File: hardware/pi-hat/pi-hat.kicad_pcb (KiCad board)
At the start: 2 copper layers, 65 x 56 mm, 83 parts, among them J1 PWR IN, J10 6-8, J11 PWM0, J12 PWM1, J13 KLPX-0848A-2-B, J14 KLPX-0848A-2-R, J2 A-F, J3 40HAT, J4 G-M, J5 N-Q, J6 PANEL_PWR, J7 PANEL_CTL, J8 2-5, J9 WP, Q1 DMG2305UX, Q2 DMMT5401, Q3 DMN6075S, Q4 NTR4171P, U1 CAT24C32, U10 L78L33_SOT89, U11 L78L33_SOT89, U12 PCM5122PW, U2 CM1293A, U3 CM1293A, U4 CM1293A, U5 CM1293A, U6 CM1293A, U7 CM1293A, U8 MCP23S17_SO, U9 MCP23S17_SO

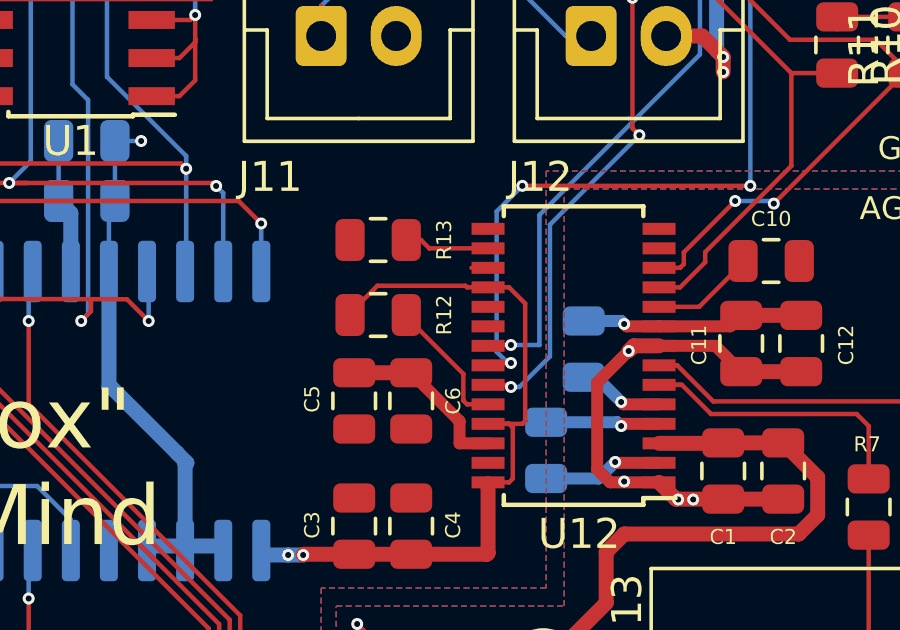
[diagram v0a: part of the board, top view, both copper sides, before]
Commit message: add jumper to optionally bridge pcm_clk and sclk as per datasheet
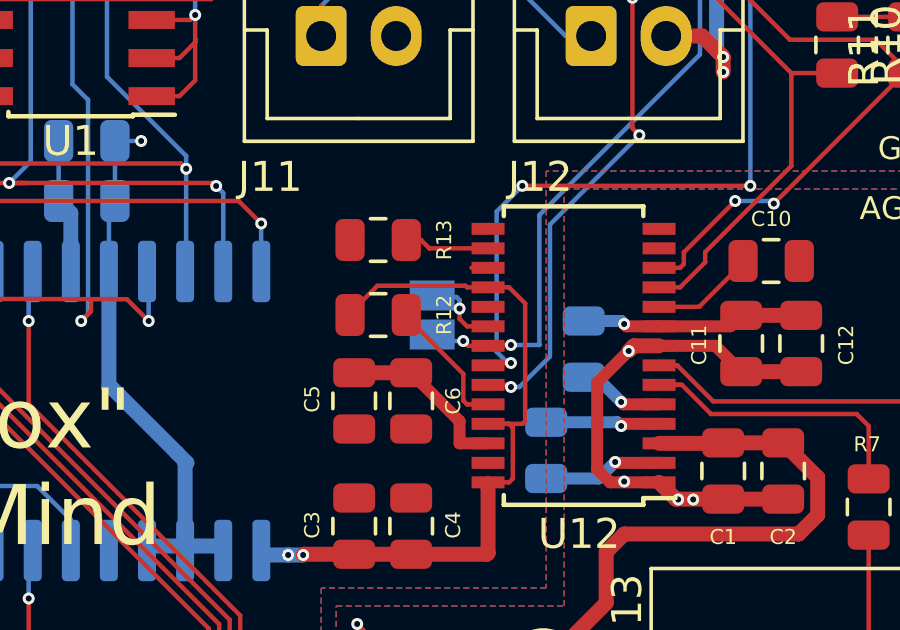
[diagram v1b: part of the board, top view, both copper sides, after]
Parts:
- added JP2: Jumper_NO_Small, Jumper:SolderJumper-2_P1.3mm_Open_Pad1.0x1.5mm, B.Cu at (125.7, 79.8)
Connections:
- U12 pad 20: (no net) -> /DAC_SYSCLK
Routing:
- net /DAC_SYSCLK: track 0.00 -> 2.66 mm, vias 0 -> 1
- net /PCM_CLK: track 58.2 -> 60.2 mm, vias 2 -> 3
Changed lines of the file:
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@@
     (thickness 1.6)
     (drawings 59)
-    (tracks 1117)
+    (tracks 1130)
     (zones 0)
-    (modules 83)
-    (nets 94)
+    (modules 84)
+    (nets 95)
   )
   (page A4)
@@
     (34 B.Paste user hide)
     (35 F.Paste user)
-    (36 B.SilkS user hide)
-    (37 F.SilkS user hide)
+    (36 B.SilkS user)
+    (37 F.SilkS user)
     (38 B.Mask user hide)
     (39 F.Mask user hide)
@@
   )
   (setup
-    (last_trace_width 0.5)
+    (last_trace_width 0.15)
     (user_trace_width 0.15)
     (user_trace_width 0.2)
@@
   (net 92 "Net-(D1-Pad2)")
   (net 93 "Net-(D1-Pad1)")
+  (net 94 /DAC_SYSCLK)
   (net_class Default "This is the default net class."
     (clearance 0.2)
@@
     (add_net /C_IN)
     (add_net /D)
+    (add_net /DAC_SYSCLK)
     (add_net /D_IN)
     (add_net /E)
@@
     (add_net "Net-(D1-Pad1)")
     (add_net "Net-(D1-Pad2)")
+    (add_net "Net-(J1-Pad2)")
+    (add_net "Net-(J1-Pad4)")
+    (add_net "Net-(J3-Pad1)")
+    (add_net "Net-(J3-Pad10)")
+    (add_net "Net-(J3-Pad11)")
+    (add_net "Net-(J3-Pad13)")
+    (add_net "Net-(J3-Pad15)")
+    (add_net "Net-(J3-Pad16)")
+    (add_net "Net-(J3-Pad26)")
+    (add_net "Net-(J3-Pad29)")
+    (add_net "Net-(J3-Pad31)")
+    (add_net "Net-(J3-Pad36)")
+    (add_net "Net-(J3-Pad37)")
+    (add_net "Net-(J3-Pad38)")
+    (add_net "Net-(J3-Pad7)")
+    (add_net "Net-(J3-Pad8)")
+    (add_net "Net-(J6-Pad3)")
+    (add_net "Net-(J7-Pad2)")
     (add_net "Net-(Q1-Pad1)")
     (add_net "Net-(Q2-Pad1)")
     (add_net "Net-(Q3-Pad1)")
     (add_net "Net-(Q4-Pad1)")
+    (add_net "Net-(U12-Pad13)")
+    (add_net "Net-(U12-Pad14)")
+    (add_net "Net-(U12-Pad15)")
+    (add_net "Net-(U12-Pad19)")
+    (add_net "Net-(U8-Pad18)")
+    (add_net "Net-(U8-Pad19)")
+    (add_net "Net-(U9-Pad19)")
+    (add_net "Net-(U9-Pad23)")
+    (add_net "Net-(U9-Pad24)")
+    (add_net "Net-(U9-Pad25)")
+    (add_net "Net-(U9-Pad26)")
+    (add_net "Net-(U9-Pad27)")
+  )
+  (module Jumper:SolderJumper-2_P1.3mm_Open_Pad1.0x1.5mm (layer B.Cu)
+    (at 125.7 79.8 270)
+    (descr "SMD Solder Jumper, 1x1.5mm Pads, 0.3mm gap, open")
+    (tags "solder jumper open")
+    (attr virtual)
+    (fp_text reference JP2 (at 0 1.5 90) (layer B.SilkS)
+      (effects (font (size 0.5 0.5) (thickness 0.125)) (justify mirror))
+    )
+    (fp_text value Jumper_NO_Small (at 0 -1.9 90) (layer B.Fab)
+      (effects (font (size 1 1) (thickness 0.15)) (justify mirror))
+    )
+    (fp_line (start 1.65 -1.25) (end -1.65 -1.25) (layer B.CrtYd) (width 0.05))
+    (fp_line (start 1.65 -1.25) (end 1.65 1.25) (layer B.CrtYd) (width 0.05))
+    (fp_line (start -1.65 1.25) (end -1.65 -1.25) (layer B.CrtYd) (width 0.05))
+    (fp_line (start -1.65 1.25) (end 1.65 1.25) (layer B.CrtYd) (width 0.05))
+    (fp_line (start -1.4 1) (end 1.4 1) (layer B.SilkS) (width 0.12))
+    (fp_line (start 1.4 1) (end 1.4 -1) (layer B.SilkS) (width 0.12))
+    (fp_line (start 1.4 -1) (end -1.4 -1) (layer B.SilkS) (width 0.12))
+    (fp_line (start -1.4 -1) (end -1.4 1) (layer B.SilkS) (width 0.12))
+    (pad 1 smd rect (at -0.65 0 270) (size 1 1.5) (layers B.Cu B.Mask)
+      (net 94 /DAC_SYSCLK))
+    (pad 2 smd rect (at 0.65 0 270) (size 1 1.5) (layers B.Cu B.Mask)
+      (net 75 /PCM_CLK))
   )
   (module TestPoint:TestPoint_Pad_D2.0mm (layer F.Cu)
@@
     (pad 21 smd rect (at 2.85 0.325 180) (size 1.1 0.4) (layers F.Cu F.Paste F.Mask)
       (net 75 /PCM_CLK))
-    (pad 20 smd rect (at 2.85 0.975 180) (size 1.1 0.4) (layers F.Cu F.Paste F.Mask))
+    (pad 20 smd rect (at 2.85 0.975 180) (size 1.1 0.4) (layers F.Cu F.Paste F.Mask)
+      (net 94 /DAC_SYSCLK))
     (pad 19 smd rect (at 2.85 1.625 180) (size 1.1 0.4) (layers F.Cu F.Paste F.Mask))
     (pad 18 smd rect (at 2.85 2.275 180) (size 1.1 0.4) (layers F.Cu F.Paste F.Mask)
@@
   (via (at 84.3 108.6) (size 0.4) (drill 0.2) (layers F.Cu B.Cu) (net 1))
   (via (at 84.8 108.6) (size 0.4) (drill 0.2) (layers F.Cu B.Cu) (net 1))
-  (via (at 123 109) (size 0.4) (drill 0.2) (layers F.Cu B.Cu) (net 6))
-  (via (at 123.5 109) (size 0.4) (drill 0.2) (layers F.Cu B.Cu) (net 6))
-  (via (at 124.2 103.8) (size 0.4) (drill 0.2) (layers F.Cu B.Cu) (net 69))
-  (via (at 133.9 85.95) (size 0.4) (drill 0.2) (layers F.Cu B.Cu) (net 69))
-  (via (at 132.1 85.35) (size 0.4) (drill 0.2) (layers F.Cu B.Cu) (net 69))
   (segment (start 133.15 112.395) (end 130.65 112.395) (width 1) (layer F.Cu) (net 1) (status 30))
   (segment (start 130.65 112.27) (end 129.09999 110.71999) (width 1) (layer F.Cu) (net 1) (status 10))
@@
   (segment (start 91.35 72.25) (end 88 72.25) (width 0.15) (layer F.Cu) (net 5))
   (segment (start 92.8 73.7) (end 91.35 72.25) (width 0.15) (layer F.Cu) (net 5) (status 10))
+  (via (at 123 109) (size 0.4) (drill 0.2) (layers F.Cu B.Cu) (net 6))
+  (via (at 123.5 109) (size 0.4) (drill 0.2) (layers F.Cu B.Cu) (net 6))
   (segment (start 80.725 69.77) (end 81.524999 69.77) (width 1) (layer F.Cu) (net 6) (status 20))
   (segment (start 83.268002 109.22) (end 81.28 109.22) (width 1) (layer F.Cu) (net 6))
@@
   (segment (start 109.75 78.445) (end 109.845 78.35) (width 0.15) (layer B.Cu) (net 68) (status 30))
   (segment (start 109.75 80) (end 109.75 78.445) (width 0.15) (layer B.Cu) (net 68) (status 20))
+  (via (at 124.2 103.8) (size 0.4) (drill 0.2) (layers F.Cu B.Cu) (net 69))
+  (via (at 133.9 85.95) (size 0.4) (drill 0.2) (layers F.Cu B.Cu) (net 69))
+  (via (at 132.1 85.35) (size 0.4) (drill 0.2) (layers F.Cu B.Cu) (net 69))
   (via (at 124.5 103.5) (size 0.4) (drill 0.2) (layers F.Cu B.Cu) (net 69))
   (segment (start 124.1865 104.5) (end 124.1865 103.8135) (width 0.5) (layer F.Cu) (net 69) (status 10))
@@
   (segment (start 129.275 80.8) (end 129.275 76.466004) (width 0.15) (layer B.Cu) (net 75))
   (segment (start 131.2 61.8) (end 131.4 61.8) (width 0.15) (layer F.Cu) (net 75))
+  (via (at 126.736067 80.666634) (size 0.4) (drill 0.2) (layers F.Cu B.Cu) (net 75))
+  (segment (start 127.563 80.828) (end 126.897433 80.828) (width 0.15) (layer F.Cu) (net 75))
+  (segment (start 126.897433 80.828) (end 126.736067 80.666634) (width 0.15) (layer F.Cu) (net 75))
+  (segment (start 125.916634 80.666634) (end 125.7 80.45) (width 0.15) (layer B.Cu) (net 75))
+  (segment (start 126.736067 80.666634) (end 125.916634 80.666634) (width 0.15) (layer B.Cu) (net 75))
   (segment (start 91.405 87.65) (end 91.405 86.625) (width 0.15) (layer B.Cu) (net 76) (status 30))
   (segment (start 91.405 86.625) (end 95.03 83) (width 0.15) (layer B.Cu) (net 76) (status 10))
@@
   (segment (start 105.925 90) (end 107.2 91.275) (width 0.15) (layer F.Cu) (net 93) (status 20))
   (segment (start 105.0875 90) (end 105.925 90) (width 0.15) (layer F.Cu) (net 93) (status 10))
+  (segment (start 126.612998 79.927998) (end 126.612998 79.584716) (width 0.15) (layer F.Cu) (net 94))
+  (via (at 126.612998 79.584716) (size 0.4) (drill 0.2) (layers F.Cu B.Cu) (net 94))
+  (segment (start 127.563 80.178) (end 126.863 80.178) (width 0.15) (layer F.Cu) (net 94))
+  (segment (start 126.863 80.178) (end 126.612998 79.927998) (width 0.15) (layer F.Cu) (net 94))
+  (segment (start 126.612998 79.301874) (end 126.511124 79.2) (width 0.15) (layer B.Cu) (net 94))
+  (segment (start 126.612998 79.584716) (end 126.612998 79.301874) (width 0.15) (layer B.Cu) (net 94))
+  (segment (start 125.75 79.2) (end 125.7 79.15) (width 0.15) (layer B.Cu) (net 94))
+  (segment (start 126.511124 79.2) (end 125.75 79.2) (width 0.15) (layer B.Cu) (net 94))
   (zone (net 1) (net_name GND) (layer F.Cu) (hatch edge 0.508)
     (connect_pads (clearance 0.2))

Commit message: final cleanup and order
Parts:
- moved J9 0.75 mm to (102.8, 72.0)
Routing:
- net /P3V3A: track 21.3 -> 21.9 mm
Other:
- board text added: "Left"
- board text added: "Right"
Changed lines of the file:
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@@
   (general
     (thickness 1.6)
-    (drawings 59)
-    (tracks 1130)
+    (drawings 61)
+    (tracks 1131)
     (zones 0)
     (modules 84)
@@
     (44 Edge.Cuts user)
     (45 Margin user hide)
-    (46 B.CrtYd user hide)
+    (46 B.CrtYd user)
     (47 F.CrtYd user)
     (48 B.Fab user hide)
@@
     (visible_elements FFFFFF7F)
     (pcbplotparams
-      (layerselection 0x010fc_ffffffff)
+      (layerselection 0x010f0_ffffffff)
       (usegerberextensions false)
       (usegerberattributes false)
@@
     (add_net "Net-(D1-Pad1)")
     (add_net "Net-(D1-Pad2)")
-    (add_net "Net-(J1-Pad2)")
-    (add_net "Net-(J1-Pad4)")
-    (add_net "Net-(J3-Pad1)")
-    (add_net "Net-(J3-Pad10)")
-    (add_net "Net-(J3-Pad11)")
-    (add_net "Net-(J3-Pad13)")
-    (add_net "Net-(J3-Pad15)")
-    (add_net "Net-(J3-Pad16)")
-    (add_net "Net-(J3-Pad26)")
-    (add_net "Net-(J3-Pad29)")
-    (add_net "Net-(J3-Pad31)")
-    (add_net "Net-(J3-Pad36)")
-    (add_net "Net-(J3-Pad37)")
-    (add_net "Net-(J3-Pad38)")
-    (add_net "Net-(J3-Pad7)")
-    (add_net "Net-(J3-Pad8)")
-    (add_net "Net-(J6-Pad3)")
-    (add_net "Net-(J7-Pad2)")
     (add_net "Net-(Q1-Pad1)")
     (add_net "Net-(Q2-Pad1)")
     (add_net "Net-(Q3-Pad1)")
     (add_net "Net-(Q4-Pad1)")
-    (add_net "Net-(U12-Pad13)")
-    (add_net "Net-(U12-Pad14)")
-    (add_net "Net-(U12-Pad15)")
-    (add_net "Net-(U12-Pad19)")
-    (add_net "Net-(U8-Pad18)")
-    (add_net "Net-(U8-Pad19)")
-    (add_net "Net-(U9-Pad19)")
-    (add_net "Net-(U9-Pad23)")
-    (add_net "Net-(U9-Pad24)")
-    (add_net "Net-(U9-Pad25)")
-    (add_net "Net-(U9-Pad26)")
-    (add_net "Net-(U9-Pad27)")
   )
   (module Jumper:SolderJumper-2_P1.3mm_Open_Pad1.0x1.5mm (layer B.Cu)
@@
     (tags diode)
     (attr smd)
-    (fp_text reference D1 (at 1.1 -1.2) (layer F.SilkS)
+    (fp_text reference D1 (at 0 -1.3) (layer F.SilkS)
       (effects (font (size 0.5 0.5) (thickness 0.125)))
     )
@@
     (tags resistor)
     (attr smd)
-    (fp_text reference R11 (at 0.0625 1.5 90) (layer F.SilkS)
-      (effects (font (size 1 1) (thickness 0.15)))
+    (fp_text reference R11 (at -2.25 0 180) (layer F.SilkS)
+      (effects (font (size 0.5 0.5) (thickness 0.125)))
     )
     (fp_text value 3.9K (at 0 1.65 90) (layer F.Fab)
@@
     (tags resistor)
     (attr smd)
-    (fp_text reference R10 (at 0 -1.65 90) (layer F.SilkS)
-      (effects (font (size 1 1) (thickness 0.15)))
+    (fp_text reference R10 (at -2.2 0 180) (layer F.SilkS)
+      (effects (font (size 0.5 0.5) (thickness 0.125)))
     )
     (fp_text value 3.9K (at 0 1.65 90) (layer F.Fab)
@@
     (tags capacitor)
     (attr smd)
-    (fp_text reference C17 (at 2.1125 0 90) (layer B.SilkS)
-      (effects (font (size 0.5 0.5) (thickness 0.125)) (justify mirror))
+    (fp_text reference C17 (at 3.3125 0 180) (layer B.SilkS)
+      (effects (font (size 1 1) (thickness 0.15)) (justify mirror))
     )
     (fp_text value .1uF (at 0 -1.65) (layer B.Fab)
@@
     (tags capacitor)
     (attr smd)
-    (fp_text reference C16 (at 2.1125 0 90) (layer B.SilkS)
-      (effects (font (size 0.5 0.5) (thickness 0.125)) (justify mirror))
+    (fp_text reference C16 (at 3.3125 0 180) (layer B.SilkS)
+      (effects (font (size 1 1) (thickness 0.15)) (justify mirror))
     )
     (fp_text value 10uF (at 0 -1.65) (layer B.Fab)
@@
     (tags resistor)
     (attr smd)
-    (fp_text reference R29 (at 0 -1.65) (layer F.SilkS)
-      (effects (font (size 1 1) (thickness 0.15)))
+    (fp_text reference R29 (at -2.15 0.05 90) (layer F.SilkS)
+      (effects (font (size 0.5 0.5) (thickness 0.125)))
     )
     (fp_text value 10K (at 0 1.65) (layer F.Fab)
@@
     (tags resistor)
     (attr smd)
-    (fp_text reference R8 (at 0 -1.65) (layer F.SilkS)
-      (effects (font (size 1 1) (thickness 0.15)))
+    (fp_text reference R8 (at -2.15 0.065 90) (layer F.SilkS)
+      (effects (font (size 0.5 0.5) (thickness 0.125)))
     )
     (fp_text value 3.9K (at 0 1.65) (layer F.Fab)
@@
     (tags resistor)
     (attr smd)
-    (fp_text reference R6 (at 0 -1.65) (layer F.SilkS)
-      (effects (font (size 1 1) (thickness 0.15)))
+    (fp_text reference R6 (at -2.15 0.05 90) (layer F.SilkS)
+      (effects (font (size 0.5 0.5) (thickness 0.125)))
     )
     (fp_text value 3.9K (at 0 1.65) (layer F.Fab)
@@
     (descr "JST XH series connector, B4B-XH-A (http://www.jst-mfg.com/product/pdf/eng/eXH.pdf), generated with kicad-footprint-generator")
     (tags "connector JST XH vertical")
-    (fp_text reference J5 (at -3.45 2.7 180) (layer F.SilkS)
+    (fp_text reference J5 (at -2.15 4.5 270) (layer F.SilkS)
       (effects (font (size 1 1) (thickness 0.15)))
     )
@@
   )
   (module Connector_PinHeader_2.54mm:PinHeader_1x02_P2.54mm_Vertical (layer F.Cu)
-    (at 103.5 72.04 180)
+    (at 102.75 72.05 180)
     (descr "Through hole straight pin header, 1x02, 2.54mm pitch, single row")
     (tags "Through hole pin header THT 1x02 2.54mm single row")
@@
       (effects (font (size 1 1) (thickness 0.15)))
     )
-    (fp_text value PWM1 (at 1.25 4.6) (layer F.Fab)
+    (fp_text value PWM1 (at 3.5 4.7) (layer F.SilkS)
       (effects (font (size 1 1) (thickness 0.15)))
     )
@@
       (effects (font (size 1 1) (thickness 0.15)))
     )
-    (fp_text value PWM0 (at 1.25 4.6) (layer F.Fab)
+    (fp_text value PWM0 (at 3.4 4.8) (layer F.SilkS)
       (effects (font (size 1 1) (thickness 0.15)))
     )
@@
     (descr "JST XH series connector, B3B-XH-A (http://www.jst-mfg.com/product/pdf/eng/eXH.pdf), generated with kicad-footprint-generator")
     (tags "connector JST XH vertical")
-    (fp_text reference J10 (at -3.4 2.3 180) (layer F.SilkS)
+    (fp_text reference J10 (at -1.7 4.7 270) (layer F.SilkS)
       (effects (font (size 1 1) (thickness 0.15)))
     )
@@
     (descr "JST XH series connector, B4B-XH-A (http://www.jst-mfg.com/product/pdf/eng/eXH.pdf), generated with kicad-footprint-generator")
     (tags "connector JST XH vertical")
-    (fp_text reference J8 (at -3.45 2.7 180) (layer F.SilkS)
+    (fp_text reference J8 (at -2.15 4.6 270) (layer F.SilkS)
       (effects (font (size 1 1) (thickness 0.15)))
     )
@@
       (clearance 1.6))
   )
+  (gr_text Right (at 125.3 99.4) (layer F.SilkS)
+    (effects (font (size 1.5 1.5) (thickness 0.3)))
+  )
+  (gr_text Left (at 125.6 97.3) (layer F.SilkS)
+    (effects (font (size 1.5 1.5) (thickness 0.3)))
+  )
   (gr_text "\"The Jukebox\"\nby MaZderMind" (at 106 84.9) (layer F.SilkS)
     (effects (font (size 2 2) (thickness 0.3)))
@@
   (gr_line (start 81.546356 116.817611) (end 140.546356 116.817611) (layer Edge.Cuts) (width 0.1))
   (gr_arc (start 140.546356 113.817611) (end 140.546356 116.817611) (angle -90) (layer Edge.Cuts) (width 0.1))
+  (via (at 125.5 103.5) (size 0.4) (drill 0.2) (layers F.Cu B.Cu) (net 69))
   (via (at 135.4 71.7) (size 0.4) (drill 0.2) (layers F.Cu B.Cu) (net 1))
   (via (at 84.3 108.6) (size 0.4) (drill 0.2) (layers F.Cu B.Cu) (net 1))
@@
   (via (at 120.9 87.8) (size 0.4) (drill 0.2) (layers F.Cu B.Cu) (net 5))
   (segment (start 120.9 87.8) (end 120.155 87.8) (width 0.5) (layer B.Cu) (net 5) (status 20))
-  (segment (start 121.4 87.8) (end 120.9 87.8) (width 0.5) (layer B.Cu) (net 5))
   (segment (start 123.87501 78.82499) (end 123.385527 79.314473) (width 0.15) (layer F.Cu) (net 5) (status 20))
   (segment (start 126.80999 78.82499) (end 123.87501 78.82499) (width 0.15) (layer F.Cu) (net 5))
@@
   (segment (start 91.35 72.25) (end 88 72.25) (width 0.15) (layer F.Cu) (net 5))
   (segment (start 92.8 73.7) (end 91.35 72.25) (width 0.15) (layer F.Cu) (net 5) (status 10))
+  (segment (start 121.4 87.8) (end 120.9 87.8) (width 0.5) (layer F.Cu) (net 5))
   (via (at 123 109) (size 0.4) (drill 0.2) (layers F.Cu B.Cu) (net 6))
   (via (at 123.5 109) (size 0.4) (drill 0.2) (layers F.Cu B.Cu) (net 6))
@@
   (segment (start 109.75 78.445) (end 109.845 78.35) (width 0.15) (layer B.Cu) (net 68) (status 30))
   (segment (start 109.75 80) (end 109.75 78.445) (width 0.15) (layer B.Cu) (net 68) (status 20))
-  (via (at 124.2 103.8) (size 0.4) (drill 0.2) (layers F.Cu B.Cu) (net 69))
   (via (at 133.9 85.95) (size 0.4) (drill 0.2) (layers F.Cu B.Cu) (net 69))
   (via (at 132.1 85.35) (size 0.4) (drill 0.2) (layers F.Cu B.Cu) (net 69))
@@
   (segment (start 131.199991 84.948533) (end 131.629458 85.378) (width 0.4) (layer F.Cu) (net 69))
   (via (at 134.4 85.95) (size 0.4) (drill 0.2) (layers F.Cu B.Cu) (net 69))
+  (segment (start 125 103.5) (end 125.6 103.5) (width 0.5) (layer F.Cu) (net 69))
   (segment (start 123.1 81.725) (end 125 81.725) (width 0.5) (layer F.Cu) (net 70) (status 30))
   (segment (start 126.612999 83.337999) (end 126.613 84.078) (width 0.4) (layer F.Cu) (net 70))

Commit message: change topology around Q4
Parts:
- added D2: ?, Diode_SMD:D_0805_2012Metric, B.Cu at (125.9, 128.1)
- added Q5: DMN6075S, Package_TO_SOT_SMD:SOT-23, B.Cu at (132.7, 131.7)
- added R15: 10k, Resistor_SMD:R_0805_2012Metric, B.Cu at (118.9, 127.5)
- added R16: 10k, Resistor_SMD:R_0805_2012Metric, B.Cu at (133.9, 125.9)
- Q4: value NTR4171P -> ?
- R23, R29: value 10K -> 10k
- R24: value 47K -> 47k
- RN1, RN2, RN3, RN4, RN5, RN6: value EXB-38V103JV -> EXB-38V100JV
- moved R3 19.9 mm to (131.0, 122.3)
- moved R4 16.5 mm to (124.6, 121.2)
- moved Q4 9.19 mm to (120.3, 123.0)
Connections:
- net Net-(D1-Pad2) renamed /LED
- Q4 pad 1: Net-(Q4-Pad1) -> Net-(D2-Pad2)
- Q4 pad 2: /PANEL_30V -> /P30V
- Q4 pad 3: /P30V -> /PANEL_30V
- R3 pad 1: Net-(Q4-Pad1) -> Net-(Q5-Pad1)
- R4 pad 1: Net-(Q4-Pad1) -> Net-(D2-Pad2)
- R4 pad 2: /P3V3 -> /P30V
- U8 pad 18: (no net) -> GND
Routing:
- net /PANEL_30V: track 14.9 -> 2.62 mm
- net Net-(Q4-Pad1): track 10.2 -> 0.00 mm
- net /P30V: track 7.96 -> 0.00 mm
- net /PANEL_SW: track 23.2 -> 17.8 mm
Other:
- board text added: "revB"
